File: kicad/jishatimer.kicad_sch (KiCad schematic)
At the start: 9 parts

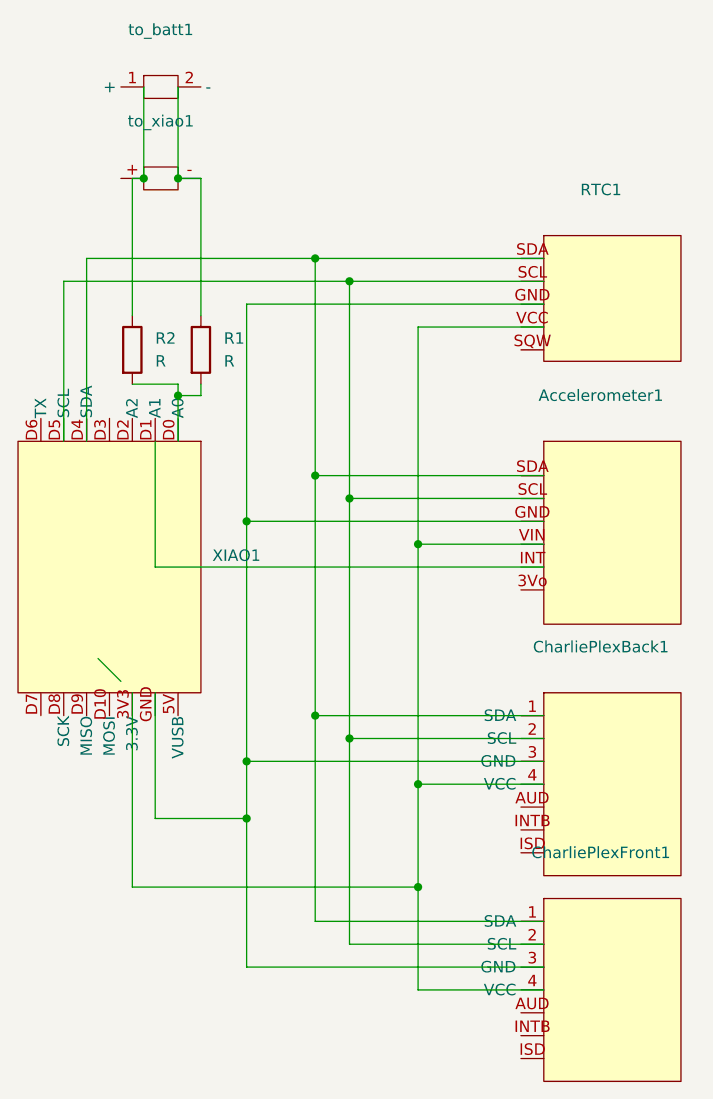
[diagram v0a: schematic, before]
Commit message: Replace LED matrix displays with single SH1106 OLED
Swap the dual IS31FL3731 LED matrix setup for one SH1106 OLED driven
via U8g2, removing the orientation-based top/bottom display switching
that's no longer needed. Also make RTC and accelerometer init
failures non-fatal so the device stays usable with degraded hardware,
and add serial diagnostic commands (X: OLED probe, I: full I2C scan)
plus a matching hardware test suite check.

Ignore KiCad's auto-generated backup/history/lock files going forward.
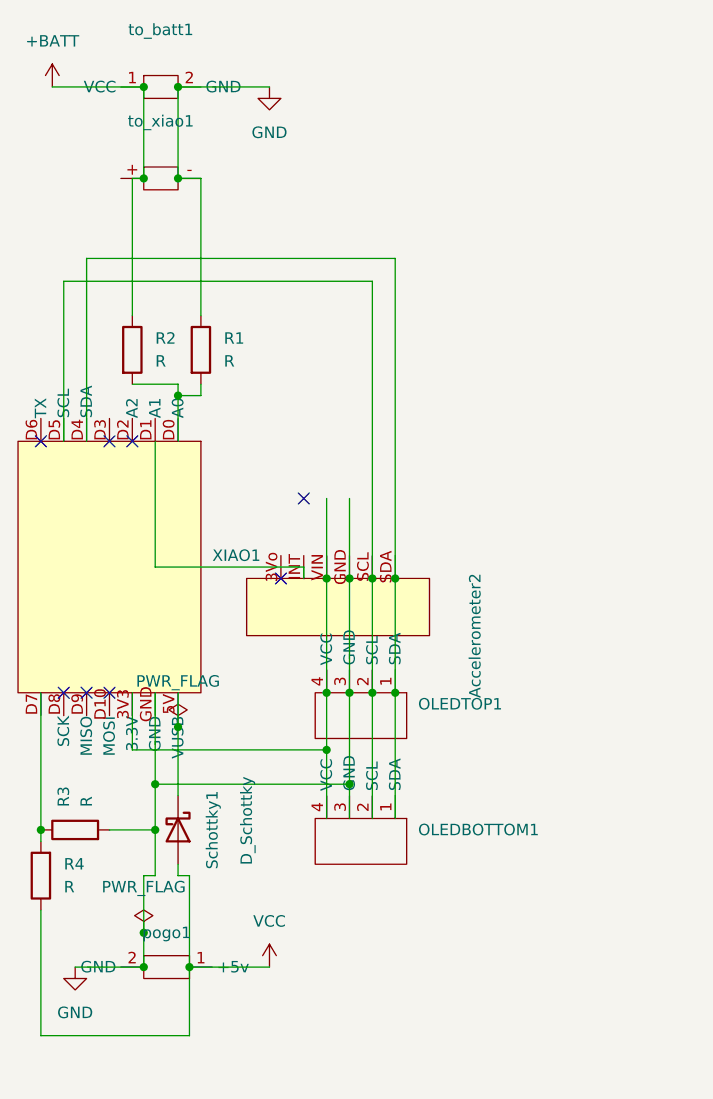
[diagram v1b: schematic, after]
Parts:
- removed Accelerometer1: ~, Alex Library:Adafruit_LIS3DH, symbol Alex Library:Adafruit_LIS3DH
- removed CharliePlexBack1, CharliePlexFront1: ~, Connector_JST:JST_PH_B4B-PH-K_1x04_P2.00mm_Vertical, symbol Alex Library:Adafruit IS31FL3731 LED Matrix driver
- removed RTC1: ~, Alex Library:Adafruit_ PCF8523, symbol Alex Library:Adafruit_PCF8523
- added Accelerometer2: (no value), Alex Library:Adafruit_LIS3DH, symbol Alex Library:Adafruit_LIS3DH
- added OLEDBOTTOM1, OLEDTOP1: (no value), Connector_JST:JST_PH_B4B-PH-K_1x04_P2.00mm_Vertical, symbol local_symbols:oled
- added R3, R4: R, Resistor_THT:R_Axial_DIN0207_L6.3mm_D2.5mm_P10.16mm_Horizontal, symbol Device:R
- added Schottky1: D_Schottky, Diode_THT:D_DO-41_SOD81_P10.16mm_Horizontal, symbol Device:D_Schottky
- added pogo1: (no value), Connector_JST:JST_PH_B2B-PH-K_1x02_P2.00mm_Vertical, symbol local_symbols:pogo_pin_input
- XIAO1, to_batt1, to_xiao1: value ~ -> (none)
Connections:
- net GND: now reaches XIAO1.GND
- net GND: now also R1.1, to_batt1.2 (GND), to_xiao1.-, Accelerometer2.GND, OLEDBOTTOM1.3 (GND), OLEDTOP1.3 (GND), R3.2, pogo1.2 (GND)
- net at XIAO1.D1 (A1): now also Accelerometer2.INT
- net at XIAO1.D5 (SCL): now also Accelerometer2.SCL, OLEDBOTTOM1.2 (SCL), OLEDTOP1.2 (SCL)
- net at XIAO1.D4 (SDA): now also Accelerometer2.SDA, OLEDBOTTOM1.1 (SDA), OLEDTOP1.1 (SDA)
- net at XIAO1.3V3 (3.3V): now also Accelerometer2.VIN, OLEDBOTTOM1.4 (VCC), OLEDTOP1.4 (VCC)
- net +BATT: now reaches R2.1, to_batt1.1 (VCC), to_xiao1.+
- net at XIAO1.D2 (A2): no longer XIAO1.
- net at XIAO1.5V (VUSB): now also Schottky1.1 (K)
- net at XIAO1.D7: now also R3.1, R4.2
- new net VCC: R4.1, Schottky1.2 (A), pogo1.1 (+5v)
- no-connect marks 0 -> 8
